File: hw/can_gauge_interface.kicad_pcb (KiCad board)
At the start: 4 copper layers, 0 parts

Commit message: buck layout
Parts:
- added C1: 22u, Capacitor_SMD:C_1206_3216Metric, F.Cu at (77.3, 78.1)
- added C10: 100n, Capacitor_SMD:C_0805_2012Metric, F.Cu at (344.4, 157.6)
- added C11: 1u, Capacitor_SMD:C_1206_3216Metric, F.Cu at (292.6, 184.6)
- added C12: 100n, Capacitor_SMD:C_0805_2012Metric, F.Cu at (348.8, 151.5)
- added C13: 100n, Capacitor_SMD:C_0805_2012Metric, F.Cu at (348.8, 154.5)
- added C14: 100n, Capacitor_SMD:C_0805_2012Metric, F.Cu at (348.8, 157.6)
- added C15: 100n, Capacitor_SMD:C_0805_2012Metric, F.Cu at (353.3, 151.5)
- added C16: 100n, Capacitor_SMD:C_0805_2012Metric, F.Cu at (353.3, 154.5)
- added C17: 100n, Capacitor_SMD:C_0805_2012Metric, F.Cu at (353.3, 157.6)
- added C18: 10u, Capacitor_SMD:C_1206_3216Metric, F.Cu at (292.6, 187.9)
- added C19: 10u, Capacitor_SMD:C_1206_3216Metric, F.Cu at (292.6, 191.3)
- added C2: 10n, Capacitor_SMD:C_0805_2012Metric, F.Cu at (83.8, 79.4)
- added C3: 22u, Capacitor_SMD:C_1206_3216Metric, F.Cu at (80.0, 64.6)
- added C4: 220p, Capacitor_SMD:C_0603_1608Metric, F.Cu at (73.0, 70.0)
- added C5: 22u, Capacitor_SMD:C_1206_3216Metric, F.Cu at (83.8, 64.6)
- added C6: 3300p, Capacitor_SMD:C_0603_1608Metric, F.Cu at (73.5, 63.5)
- added C7: 47n, Capacitor_SMD:C_0805_2012Metric, F.Cu at (72.4, 66.0)
- added C8: 10u, Capacitor_SMD:C_1206_3216Metric, F.Cu at (292.6, 177.9)
- added C9: 10u, Capacitor_SMD:C_1206_3216Metric, F.Cu at (292.6, 181.2)
- added D1: SS34, Diode_SMD:D_SMA, F.Cu at (83.2, 73.8)
- added H1: MountingHole, MountingHole:MountingHole_3.2mm_M3_DIN965, F.Cu at (329.2, 183.8)
- added H2: MountingHole, MountingHole:MountingHole_3.2mm_M3_DIN965, F.Cu at (329.2, 191.0)
- added H3: MountingHole, MountingHole:MountingHole_3.2mm_M3_DIN965, F.Cu at (329.2, 198.2)
- added H4: MountingHole, MountingHole:MountingHole_3.2mm_M3_DIN965, F.Cu at (329.2, 205.3)
- added J1: USB_B, Connector_USB:USB_B_Lumberg_2411_02_Horizontal, F.Cu at (63.3, 192.7)
- added J10: +5VA, Connector_PinSocket_2.54mm:PinSocket_1x01_P2.54mm_Vertical, F.Cu at (356.7, 191.8)
- added J2: Conn_02x04_Top_Bottom, Connector_Molex:Molex_Mini-Fit_Jr_5569-08A2_2x04_P4.20mm_Horizontal, F.Cu at (63.1, 165.1)
- added J3: Analog, Connector_Molex:Molex_Mini-Fit_Jr_5569-06A2_2x03_P4.20mm_Horizontal, F.Cu at (63.1, 252.2)
- added J4: ICSP, Connector_PinHeader_2.54mm:PinHeader_1x05_P2.54mm_Vertical, F.Cu at (322.9, 187.8)
- added J5: SPI Debug, Connector_PinSocket_2.54mm:PinSocket_1x03_P2.54mm_Vertical, F.Cu at (345.9, 204.5)
- added J6: CAN ~{CS}, Connector_PinSocket_2.54mm:PinSocket_1x01_P2.54mm_Vertical, F.Cu at (356.7, 182.6)
- added J7: ROM ~{CS}, Connector_PinSocket_2.54mm:PinSocket_1x01_P2.54mm_Vertical, F.Cu at (356.7, 187.2)
- added J8: DAC ~{CS}, Connector_PinSocket_2.54mm:PinSocket_1x02_P2.54mm_Vertical, F.Cu at (333.7, 145.2)
- added J9: Conn_01x04_Socket, Connector_PinSocket_2.54mm:PinSocket_1x04_P2.54mm_Vertical, F.Cu at (322.9, 202.7)
- added JP2: Prog, Connector_PinSocket_2.54mm:PinSocket_1x03_P2.54mm_Vertical, F.Cu at (350.5, 204.5)
- added JP3: USB_PWR, Connector_PinSocket_2.54mm:PinSocket_1x02_P2.54mm_Vertical, F.Cu at (338.3, 145.2)
- added JP4: USB_PWR, Connector_PinSocket_2.54mm:PinSocket_1x02_P2.54mm_Vertical, F.Cu at (342.9, 145.2)
- added JP5: Term, Connector_PinSocket_2.54mm:PinSocket_1x02_P2.54mm_Vertical, F.Cu at (347.5, 145.2)
- added L1: 150u, Inductor_SMD:L_12x12mm_H8mm, F.Cu at (92.7, 69.2)
- added R1: 10k, Resistor_SMD:R_0805_2012Metric, F.Cu at (73.4, 61.0)
- added R10: 10k, Resistor_SMD:R_0805_2012Metric, F.Cu at (306.4, 187.0)
- added R11: 10k, Resistor_SMD:R_0805_2012Metric, F.Cu at (306.4, 189.9)
- added R2: 3k24, Resistor_SMD:R_0805_2012Metric, F.Cu at (66.7, 69.6)
- added R3: 2k7, Resistor_SMD:R_0805_2012Metric, F.Cu at (69.8, 69.8)
- added R6: 10k, Resistor_SMD:R_0805_2012Metric, F.Cu at (302.0, 184.0)
- added R7: 10k, Resistor_SMD:R_0805_2012Metric, F.Cu at (302.0, 187.0)
- added R8: 120, Resistor_SMD:R_0805_2012Metric, F.Cu at (302.0, 189.9)
- added R9: 10k, Resistor_SMD:R_0805_2012Metric, F.Cu at (306.4, 184.0)
- added SW1: Reset, Button_Switch_THT:SW_PUSH-12mm, F.Cu at (291.9, 198.2)
- added U1: PIC16F1459-IP, Package_DIP:DIP-20_W7.62mm, F.Cu at (243.8, 124.5)
- added U2: MCP2515-I/P, Package_DIP:DIP-18_W7.62mm, F.Cu at (334.4, 182.3)
- added U3: MCP2561-E-P, Package_DIP:DIP-8_W7.62mm, F.Cu at (333.0, 152.1)
- added U4: 25LC160C, Package_DIP:DIP-8-16_W7.62mm, F.Cu at (345.2, 182.3)
- added U5: TPS5430DDA, Package_SO:TI_SO-PowerPAD-8_ThermalVias, F.Cu at (77.5, 71.9)
- added U6: L78M05AB, Package_TO_SOT_SMD:TO-252-2, F.Cu at (302.3, 170.3)
- added U7: L78M05AB, Package_TO_SOT_SMD:TO-252-2, F.Cu at (302.3, 178.5)
- added U8: MCP4912, Package_DIP:DIP-14_W7.62mm, F.Cu at (311.4, 144.9)
- added U9: MCP4912, Package_DIP:DIP-14_W7.62mm, F.Cu at (322.2, 144.9)

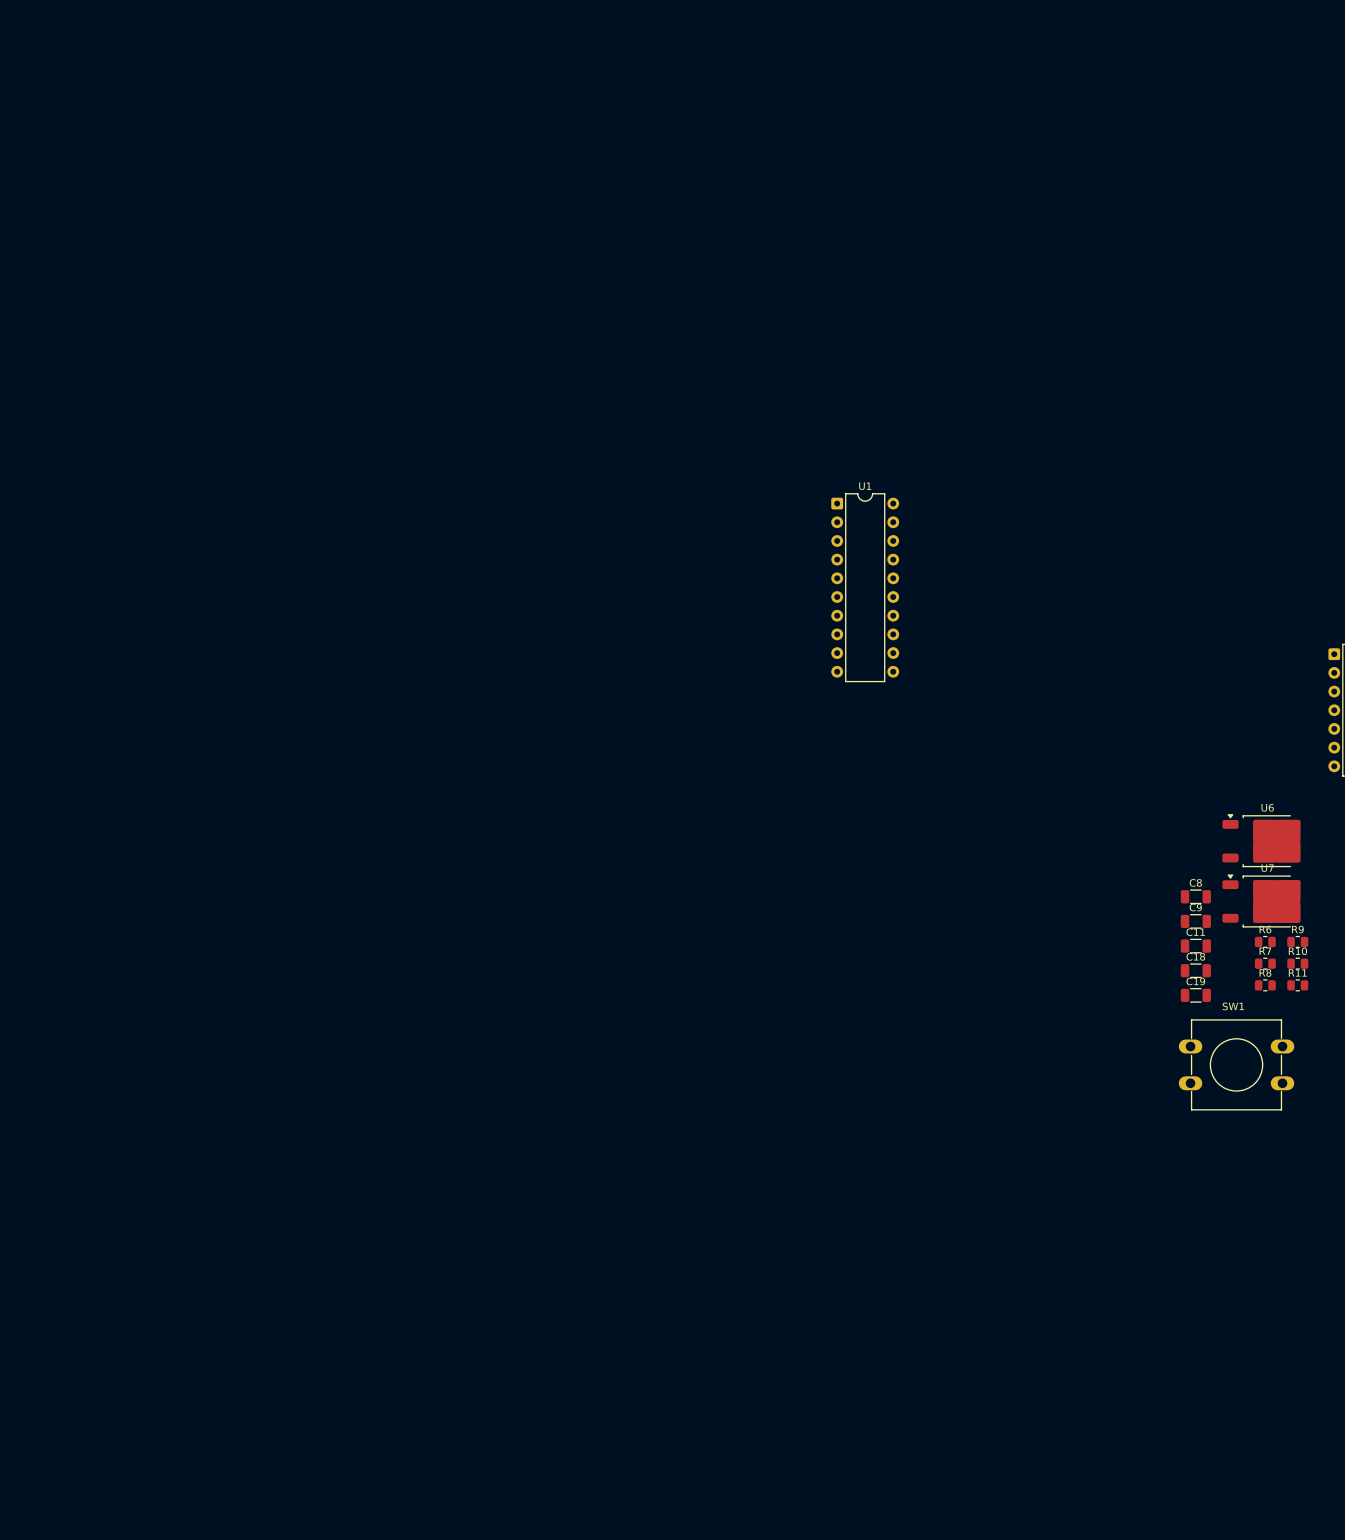
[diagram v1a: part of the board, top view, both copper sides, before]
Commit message: ldo layout
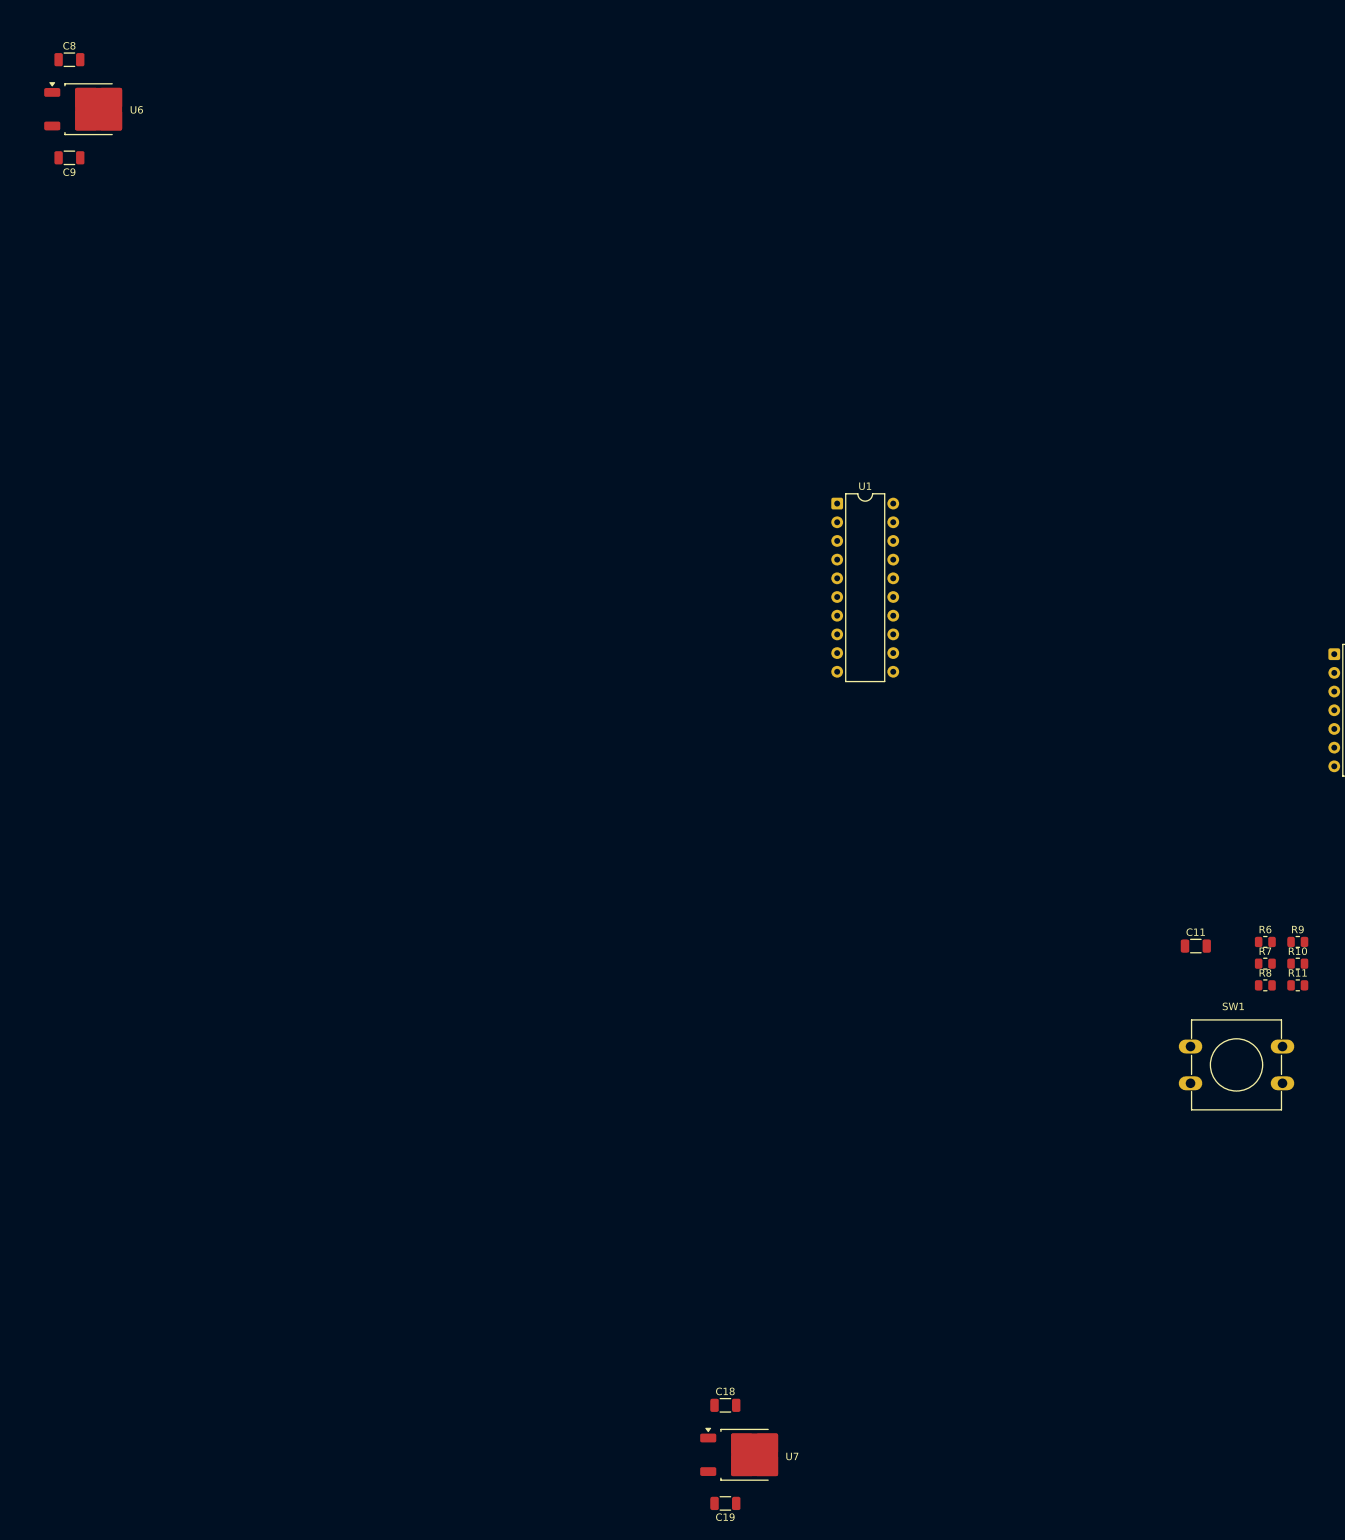
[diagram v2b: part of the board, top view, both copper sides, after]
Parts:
- moved C8 190.7 mm to (139.5, 64.1)
- moved U6 188.5 mm to (142.2, 70.9)
- moved C9 185.0 mm to (139.5, 77.5)
- moved U7 103.4 mm to (231.4, 253.7)
- moved C19 94.1 mm to (228.6, 260.4)
- moved C18 87.0 mm to (228.6, 247.0)
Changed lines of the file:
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@@
 	(footprint "Capacitor_SMD:C_1206_3216Metric"
 		(layer "F.Cu")
-		(at 292.59 181.25)
+		(at 139.495 77.47)
 		(descr "Capacitor SMD 1206 (3216 Metric), square (rectangular) end terminal, IPC_7351 nominal, (Body size source: IPC-SM-782 page 76, https://www.pcb-3d.com/wordpress/wp-content/uploads/ipc-sm-782a_amendment_1_and_2.pdf), generated with kicad-footprint-generator")
 		(tags "capacitor")
 		(property "Reference" "C9"
-			(at 0 -1.85 0)
+			(at 0 1.984 0)
 			(layer "F.SilkS")
 			(effects
@@
 			(at 0 1.85 0)
 			(layer "F.Fab")
+			(hide yes)
 			(effects
 				(font
@@
 	(footprint "Capacitor_SMD:C_1206_3216Metric"
 		(layer "F.Cu")
-		(at 292.59 191.3)
+		(at 228.649 260.35)
 		(descr "Capacitor SMD 1206 (3216 Metric), square (rectangular) end terminal, IPC_7351 nominal, (Body size source: IPC-SM-782 page 76, https://www.pcb-3d.com/wordpress/wp-content/uploads/ipc-sm-782a_amendment_1_and_2.pdf), generated with kicad-footprint-generator")
 		(tags "capacitor")
 		(property "Reference" "C19"
-			(at 0 -1.85 0)
+			(at 0 1.905 0)
 			(layer "F.SilkS")
 			(effects
@@
 			(at 0 1.85 0)
 			(layer "F.Fab")
+			(hide yes)
 			(effects
 				(font
@@
 	(footprint "Capacitor_SMD:C_1206_3216Metric"
 		(layer "F.Cu")
-		(at 292.59 187.95)
+		(at 228.649 247.015)
 		(descr "Capacitor SMD 1206 (3216 Metric), square (rectangular) end terminal, IPC_7351 nominal, (Body size source: IPC-SM-782 page 76, https://www.pcb-3d.com/wordpress/wp-content/uploads/ipc-sm-782a_amendment_1_and_2.pdf), generated with kicad-footprint-generator")
 		(tags "capacitor")
@@
 			(at 0 1.85 0)
 			(layer "F.Fab")
+			(hide yes)
 			(effects
 				(font
@@
 	(footprint "Package_TO_SOT_SMD:TO-252-2"
 		(layer "F.Cu")
-		(at 302.33 170.345)
+		(at 142.2 70.86)
 		(descr "TO-252/DPAK SMD package, http://www.infineon.com/cms/en/product/packages/PG-TO252/PG-TO252-3-1/")
 		(tags "DPAK TO-252 DPAK-3 TO-252-3 SOT-428")
 		(property "Reference" "U6"
-			(at 0 -4.5 0)
+			(at 6.443 0.128 0)
 			(layer "F.SilkS")
 			(effects
@@
 			(at 0 4.5 0)
 			(layer "F.Fab")
+			(hide yes)
 			(effects
 				(font
@@
 	(footprint "Capacitor_SMD:C_1206_3216Metric"
 		(layer "F.Cu")
-		(at 292.59 177.9)
+		(at 139.495 64.135)
 		(descr "Capacitor SMD 1206 (3216 Metric), square (rectangular) end terminal, IPC_7351 nominal, (Body size source: IPC-SM-782 page 76, https://www.pcb-3d.com/wordpress/wp-content/uploads/ipc-sm-782a_amendment_1_and_2.pdf), generated with kicad-footprint-generator")
 		(tags "capacitor")
@@
 			(at 0 1.85 0)
 			(layer "F.Fab")
+			(hide yes)
 			(effects
 				(font
@@
 	(footprint "Package_TO_SOT_SMD:TO-252-2"
 		(layer "F.Cu")
-		(at 302.33 178.54)
+		(at 231.354 253.74)
 		(descr "TO-252/DPAK SMD package, http://www.infineon.com/cms/en/product/packages/PG-TO252/PG-TO252-3-1/")
 		(tags "DPAK TO-252 DPAK-3 TO-252-3 SOT-428")
 		(property "Reference" "U7"
-			(at 0 -4.5 0)
+			(at 6.39 0.26 0)
 			(layer "F.SilkS")
 			(effects
@@
 			(at 0 4.5 0)
 			(layer "F.Fab")
+			(hide yes)
 			(effects
 				(font

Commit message: can layout
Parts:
- moved JP5 267.8 mm to (80.0, 157.5), turned to 180 degrees
- moved C14 261.0 mm to (88.0, 166.4)
- moved C13 249.0 mm to (100.0, 146.1), turned to 180 degrees
- moved U3 239.2 mm to (94.0, 162.6), turned to 180 degrees
- moved U2 236.6 mm to (99.1, 157.5), turned to 90 degrees
- moved R8 229.8 mm to (74.9, 154.9), turned to 90 degrees
- moved R7 206.7 mm to (100.1, 142.9)

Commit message: pic layout
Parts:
- U4: footprint Package_DIP:DIP-8-16_W7.62mm -> Package_DIP:DIP-8_W7.62mm
- moved C12 233.5 mm to (115.6, 162.2), turned to -90 degrees
- moved U4 232.8 mm to (116.8, 137.2), turned to -90 degrees
- moved C15 232.8 mm to (120.7, 143.8), turned to -90 degrees
- moved C10 216.3 mm to (128.3, 148.6)
- moved R9 207.3 mm to (104.1, 138.8), turned to -90 degrees
- moved R6 192.5 mm to (110.8, 161.3)
- moved SW1 181.7 mm to (111.8, 173.9), turned to 180 degrees
- moved C11 159.3 mm to (135.9, 156.2), turned to 90 degrees
- moved U1 122.6 mm to (124.5, 152.4)
- moved J1 55.5 mm to (64.8, 137.2)
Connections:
- U1 pad 10: /DAC1_~{CS} -> unconnected-(U1-RB7/TX/CK-Pad10)
- U1 pad 12: /ROM_~{CS} -> unconnected-(U1-RB5/AN11/RX/DX-Pad12)
- U1 pad 2: /DAC2_~{CS} -> /CAN_~{CS}
- U1 pad 6: /Speed -> unconnected-(U1-CWG1B/C1OUT/C2OUT/RC4-Pad6)
- U1 pad 7: /Tach -> unconnected-(U1-CLKR/C1IN3-/C2IN3-/DACOUT2/AN7/RC3-Pad7)
- U1 pad 8: /CAN_~{CS} -> unconnected-(U1-~{SS}/PWM2/AN8/RC6-Pad8)

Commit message: tht passives
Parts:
- C10, C12, C13, C14, C15, C16, C17: footprint Capacitor_SMD:C_0805_2012Metric -> Capacitor_THT:C_Disc_D5.0mm_W2.5mm_P2.50mm
- R10, R11, R6, R7, R9: footprint Resistor_SMD:R_0805_2012Metric -> Resistor_THT:R_Axial_DIN0207_L6.3mm_D2.5mm_P7.62mm_Horizontal
- moved R9 23.6 mm to (127.0, 144.8), turned to 90 degrees
- moved C14 11.7 mm to (97.8, 160.0), turned to 90 degrees
- moved R6 4.17 mm to (106.7, 161.3)
- moved C13 4.08 mm to (104.1, 146.1)
- moved C12 3.93 mm to (119.4, 161.3)
- moved U4 3.59 mm to (119.4, 139.7)
- moved C15 2.98 mm to (123.2, 142.3)
- moved C11 2.54 mm to (138.4, 156.2)
- moved U1 2.54 mm to (127.0, 152.4)
- moved SW1 2.54 mm to (114.3, 173.9)
- moved U2 2.54 mm to (101.6, 157.5)
- moved C19 1.27 mm to (228.6, 259.1)
- moved C18 1.27 mm to (228.6, 248.3)
- moved C8 1.27 mm to (139.5, 65.4)
- moved C9 1.27 mm to (139.5, 76.2)
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
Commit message: layout
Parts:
- moved H4 291.2 mm to (55.0, 107.5)
- moved H1 274.9 mm to (55.0, 202.5)
- moved C17 261.2 mm to (95.2, 198.1), turned to -90 degrees
- moved J6 255.8 mm to (104.1, 142.2)
- moved J9 253.2 mm to (81.3, 127.0), turned to 90 degrees
- moved J5 245.9 mm to (111.8, 129.5), turned to 90 degrees
- moved J7 239.3 mm to (124.5, 129.5)
- moved C16 239.2 mm to (118.1, 198.1), turned to -90 degrees
- moved U9 235.7 mm to (91.4, 193.0), turned to -90 degrees
- moved J8 228.1 mm to (109.2, 185.4), turned to -90 degrees
- moved JP2 214.9 mm to (144.8, 142.2), turned to 180 degrees
- moved R11 212.5 mm to (94.0, 190.5), turned to 180 degrees
- moved H3 207.6 mm to (142.5, 107.5)
- moved U8 202.9 mm to (114.3, 193.0), turned to -90 degrees
- moved J4 192.5 mm to (145.0, 114.3)
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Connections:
- U1 pad 5: unconnected-(U1-PWM1/CWG1A/T0CKI/RC5-Pad5) -> /ROM_~{CS}
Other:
- board outline added: 97.5 x 105 mm
- board text added: "12 7 5 GND"
- board text added: "MOSI SCK MISO"
- board text added: "SPI"

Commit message: buck routing
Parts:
- moved JP4 269.2 mm to (73.7, 144.8), turned to -90 degrees
- moved JP3 264.7 mm to (73.7, 139.7), turned to 90 degrees
- moved J10 232.3 mm to (124.5, 198.1)
- moved JP2 23.0 mm to (142.2, 119.4)
- moved J4 21.9 mm to (124.5, 106.7), turned to 90 degrees
- moved C18 4.68 mm to (132.6, 188.9)
- moved C19 4.68 mm to (132.6, 199.7)
- moved U7 4.68 mm to (135.3, 194.3)
- moved J8 2.54 mm to (111.8, 185.4)
- moved C11 1.29 mm to (137.2, 156.4)
- moved R1 1.27 mm to (63.2, 105.4)
- moved C6 0.64 mm to (63.4, 108.6)
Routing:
- net /sense: track 0.00 -> 22.2 mm
- net /PH: track 0.00 -> 19.1 mm
- net Net-(U5-BOOT): track 0.00 -> 13.3 mm, vias 0 -> 2
- net +7V: track 0.00 -> 8.00 mm
- net +12V: track 0.00 -> 3.75 mm, vias 0 -> 1
- net Net-(C7-Pad2): track 0.00 -> 3.56 mm
- net GND: vias 0 -> 23
- added copper zone on F.Cu, net +5V
- added copper zone on F.Cu, net +7V
- added copper zone on F.Cu, net GND
- added copper zone on In1.Cu, net GND
- added copper zone on In2.Cu, net GND

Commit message: routing
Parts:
- moved J8 2.84 mm to (114.3, 186.7)
- moved C18 2.29 mm to (134.9, 188.8)
- moved C19 2.29 mm to (134.9, 199.6)
- moved U7 2.29 mm to (137.6, 194.3)
- moved J5 1.27 mm to (110.5, 129.5)
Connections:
- U1 pad 10: unconnected-(U1-RB7/TX/CK-Pad10) -> /DAC2_~{CS}
- U1 pad 12: unconnected-(U1-RB5/AN11/RX/DX-Pad12) -> /DAC1_~{CS}
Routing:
- net /SCK: track 0.00 -> 184.4 mm
- net /MOSI: track 0.00 -> 176.4 mm, vias 0 -> 3
- net /USB_D+: track 0.00 -> 111.3 mm
- net /USB_D-: track 0.00 -> 109.9 mm, vias 0 -> 1
- net /DAC1_~{CS}: track 0.00 -> 42.1 mm
- net /MISO: track 0.00 -> 30.6 mm
- net /CAN_~{CS}: track 0.00 -> 23.5 mm
- net /~{MCLR}: track 0.00 -> 20.8 mm
- net /CLK: track 0.00 -> 9.20 mm
- net GND: vias 23 -> 53
- net +7V: vias 0 -> 1
- added copper zone on F.Cu, net +5VA
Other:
- board text added: "DAC1 ~{CS}"
- board text added: "DAC2 ~{CS}"
